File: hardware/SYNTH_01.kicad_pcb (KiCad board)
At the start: 2 copper layers, 55 parts, among them J2 Conn_01x04_Pin, SW1 SW_Push_45deg, SW10 SW_Push_45deg, SW11 SW_Push_45deg, SW12 SW_Push_45deg, SW13 SW_Push_45deg, SW14 SW_Push_45deg, SW15 SW_Push_45deg, SW16 SW_Push_45deg, SW17 SW_Push_45deg, SW18 SW_Push_45deg, SW19 SW_Push_45deg, SW2 SW_Push_45deg, SW20 SW_Push_45deg, SW21 SW_Push_45deg, SW3 SW_Push_45deg, SW4 SW_Push_45deg, SW5 SW_Push_45deg, SW6 SW_Push_45deg, SW7 SW_Push_45deg, SW8 SW_Push_45deg, SW9 SW_Push_45deg, U1 MCP23017-E/SP

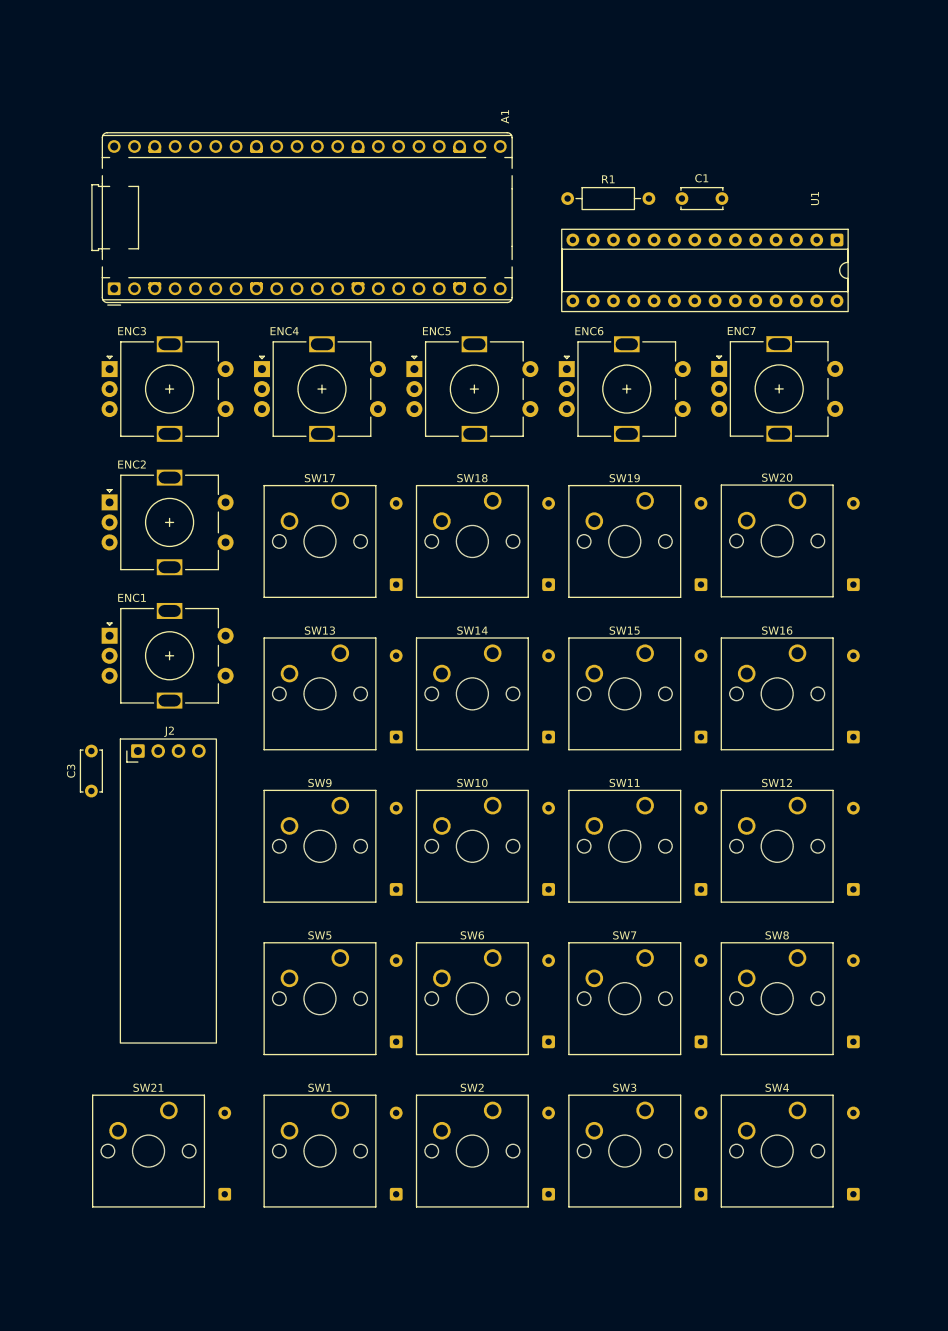
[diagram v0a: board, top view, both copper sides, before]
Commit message: PCB: linking encoders GND in PCB view, adding GND thermal to board
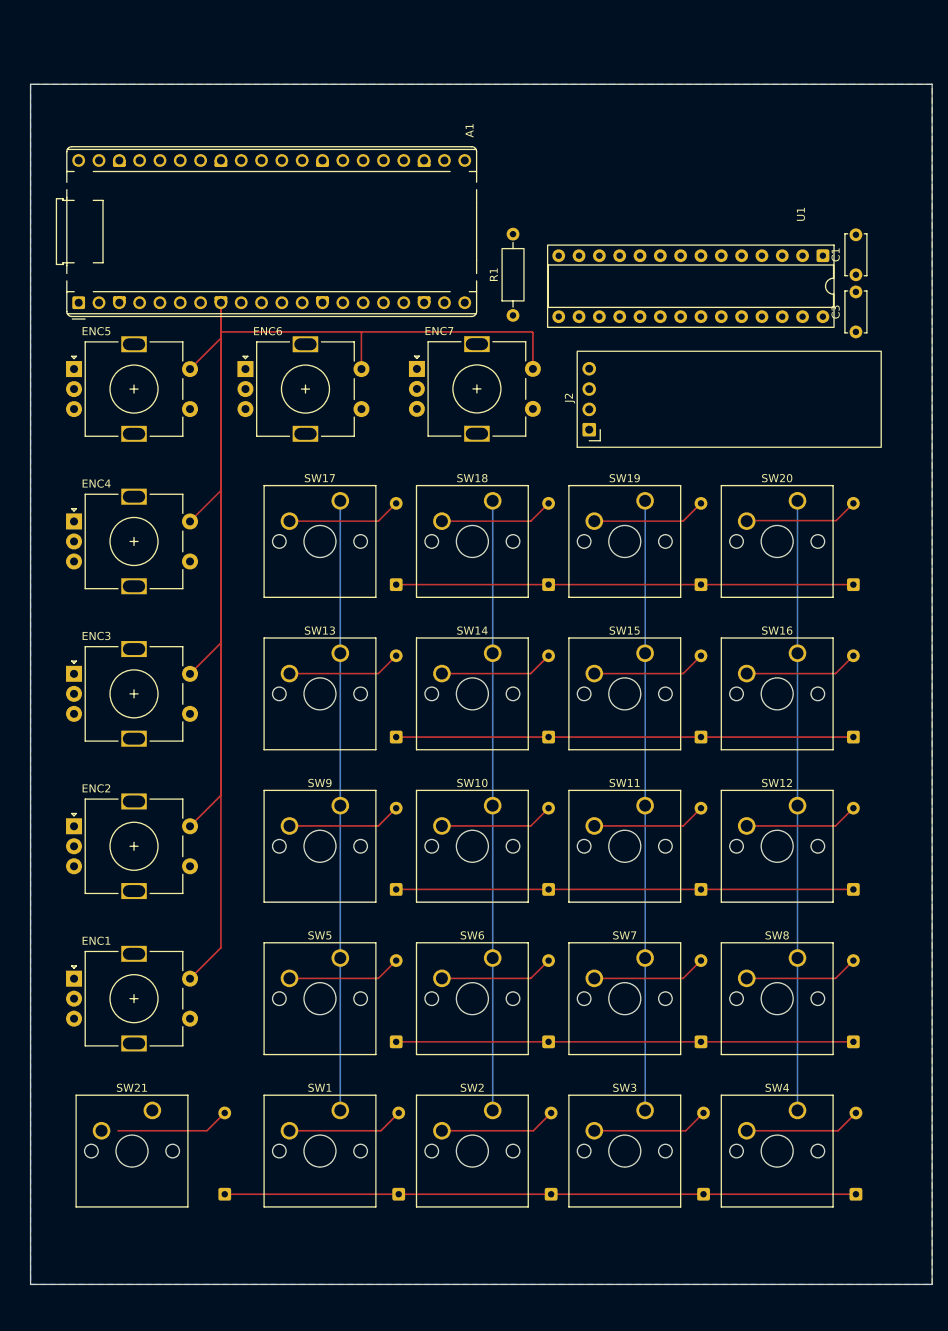
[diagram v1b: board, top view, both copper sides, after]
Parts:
- moved C3 111.5 mm to (147.6, 59.5)
- moved J2 69.3 mm to (114.3, 71.8), turned to 90 degrees
- moved D4 57.5 mm to (147.6, 167.3)
- moved D1 56.8 mm to (90.5, 167.3)
- moved ENC1 43.1 mm to (49.9, 140.4)
- moved ENC5 42.5 mm to (49.9, 64.2)
- moved ENC2 40.7 mm to (49.9, 121.3)
- moved ENC6 40.2 mm to (71.3, 64.2)
- moved ENC3 38.4 mm to (49.9, 102.3)
- moved ENC7 37.8 mm to (92.8, 64.2)
- moved ENC4 30.2 mm to (49.9, 83.2)
- moved C1 23.7 mm to (147.6, 52.4), turned to 90 degrees
- moved D3 19.4 mm to (128.6, 167.3)
- moved D2 18.7 mm to (109.5, 167.3)
- moved R1 16.1 mm to (104.8, 57.5), turned to 90 degrees
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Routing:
- net GND: track 0.00 -> 288.2 mm
- net /ROW4: track 0.00 -> 78.9 mm
- net /COL3: track 0.00 -> 76.3 mm
- net /COL2: track 0.00 -> 76.2 mm
- net /COL1: track 0.00 -> 76.2 mm
- net /COL0: track 0.00 -> 76.2 mm
- net /ROW3: track 0.00 -> 57.1 mm
- net /ROW2: track 0.00 -> 57.1 mm
- net /ROW1: track 0.00 -> 57.1 mm
- net /ROW0: track 0.00 -> 57.1 mm
- net Net-(D1-A): track 0.00 -> 14.6 mm
- net Net-(D3-A): track 0.00 -> 14.6 mm
- net Net-(D2-A): track 0.00 -> 14.6 mm
- net Net-(D4-A): track 0.00 -> 14.6 mm
- net Net-(D9-A): track 0.00 -> 14.3 mm
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- added copper zone on B.Cu, net GND
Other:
- board outline added: 112.7 x 150 mm

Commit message: fix: establish no-led PCB routing checkpoint
Prepare the pre-RGB SYNTH_01 variant on branch no_led for continued manual KiCad routing.\n\n- Add and wire the 4.7 kOhm DNP I2C pull-ups from +3V3 to SDA/SCL.\n- Validate the Pico/MCP power, reset, I2C and ground connections in the schematic.\n- Synchronize the PCB and route the power, I2C, reset and complete encoder subsystem.\n- Keep the RGB subsystem out of this buildable no-led variant.\n\nVerification at checkpoint time: schematic ERC reports 0 violations and schematic/PCB parity is clean. All 21 encoder nets are connected. PCB DRC reports 17 unconnected items: 10 matrix nets and 7 GND connections. It also reports 29 violations: 21 isolated-copper warnings, 4 starved-thermal warnings and 4 silkscreen overlaps. This checkpoint is not a fabrication release.
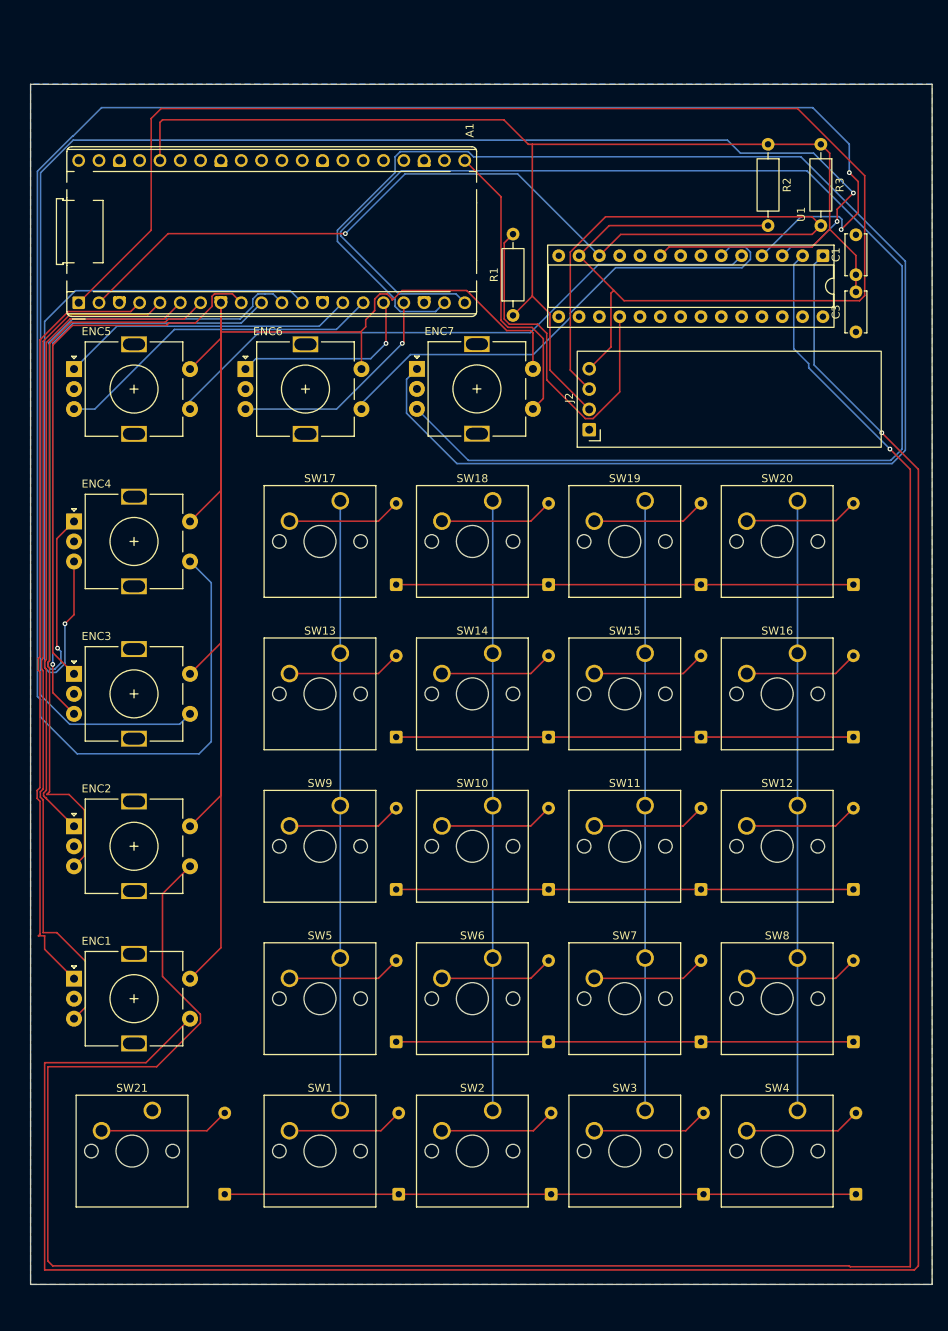
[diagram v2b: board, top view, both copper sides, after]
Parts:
- added R2: 4.7k, Resistor_THT:R_Axial_DIN0207_L6.3mm_D2.5mm_P10.16mm_Horizontal, F.Cu at (136.7, 36.1)
- added R3: 4.7k, Resistor_THT:R_Axial_DIN0207_L6.3mm_D2.5mm_P10.16mm_Horizontal, F.Cu at (143.3, 36.1)
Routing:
- net /E2_SW: track 0.00 -> 309.6 mm, vias 0 -> 1
- net /E1_SW: track 0.00 -> 287.9 mm, vias 0 -> 1
- net /E4_SW: track 0.00 -> 248.0 mm, vias 0 -> 2
- net /SDA: track 0.00 -> 209.5 mm
- net /E3_SW: track 0.00 -> 205.1 mm, vias 0 -> 2
- net /E7_A: track 0.00 -> 196.7 mm
- net /E7_B: track 0.00 -> 184.6 mm
- net +3V3: track 0.00 -> 171.1 mm
- net /SCL: track 0.00 -> 154.4 mm, vias 0 -> 1
- net /E1_B: track 0.00 -> 105.5 mm
- net /E1_A: track 0.00 -> 97.1 mm
- net /E4_B: track 0.00 -> 94.2 mm, vias 0 -> 1
- net /E4_A: track 0.00 -> 94.1 mm, vias 0 -> 1
- net /E2_B: track 0.00 -> 90.7 mm
- net /E2_A: track 0.00 -> 81.2 mm
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
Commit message: PCB: add 4 mounting holes and partial GND block (checkpoint for resume)
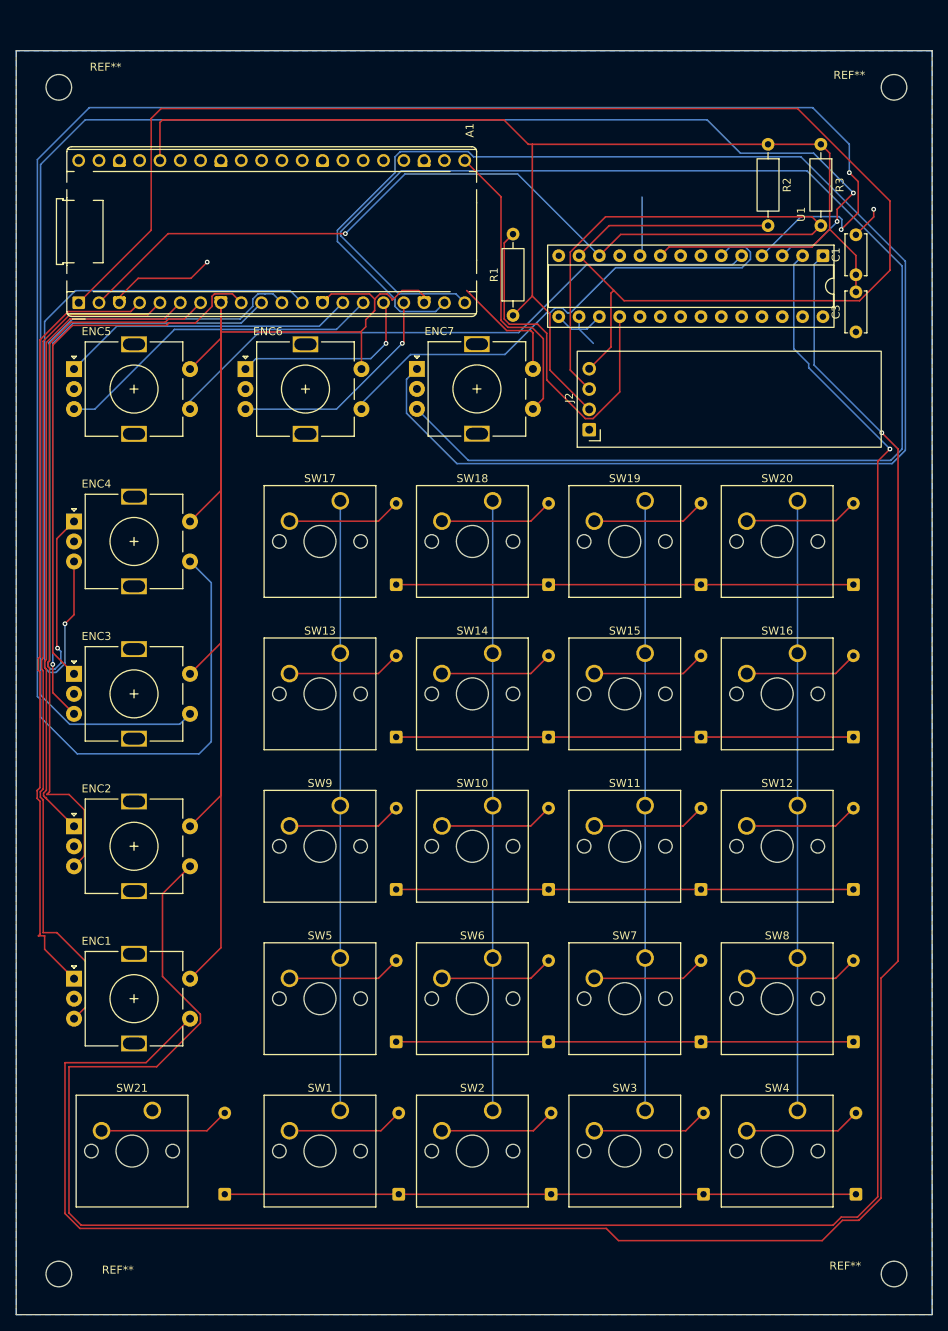
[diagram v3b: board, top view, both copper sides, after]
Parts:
- added REF**: MountingHole_3.2mm_M3, MountingHole:MountingHole_3.2mm_M3, F.Cu at (152.4, 177.3)
- added REF**: MountingHole_3.2mm_M3, MountingHole:MountingHole_3.2mm_M3, F.Cu at (48.0, 29.0)
- added REF**: MountingHole_3.2mm_M3, MountingHole:MountingHole_3.2mm_M3, F.Cu at (152.4, 29.0)
- added REF**: MountingHole_3.2mm_M3, MountingHole:MountingHole_3.2mm_M3, F.Cu at (48.0, 177.3)
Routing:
- net GND: track 294.6 -> 333.6 mm, vias 0 -> 2
- net /E2_SW: track 309.6 -> 286.9 mm
- net /E1_SW: track 287.9 -> 265.9 mm
- net /E3_SW: track 205.1 -> 207.8 mm
- net /SDA: track 209.5 -> 212.1 mm
- net /E4_SW: track 248.0 -> 248.9 mm
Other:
- board size 112.7 x 150 mm -> 114.5 x 158 mm

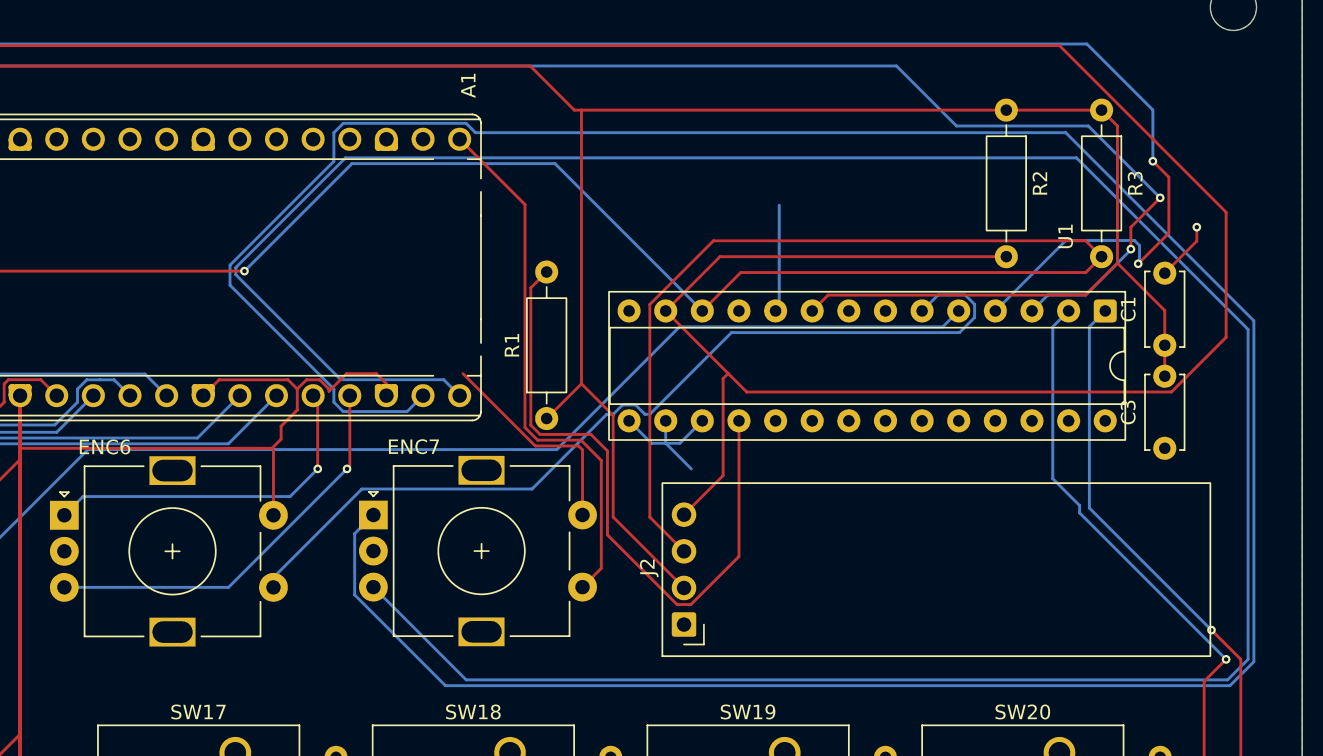
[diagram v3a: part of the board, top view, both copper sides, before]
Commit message: fix(pcb): consolidate GND-plane checkpoint
Remove floating B.Cu GND islands and complete the Pico ground return.

DRC checkpoint: 10 unrouted matrix nets remain; 6 starved thermals and 4
silkscreen overlaps remain. No GND missing connection, short circuit, or
dangling track remains. Resume by routing the matrix, then repair thermals
and silkscreen before Gerber review.
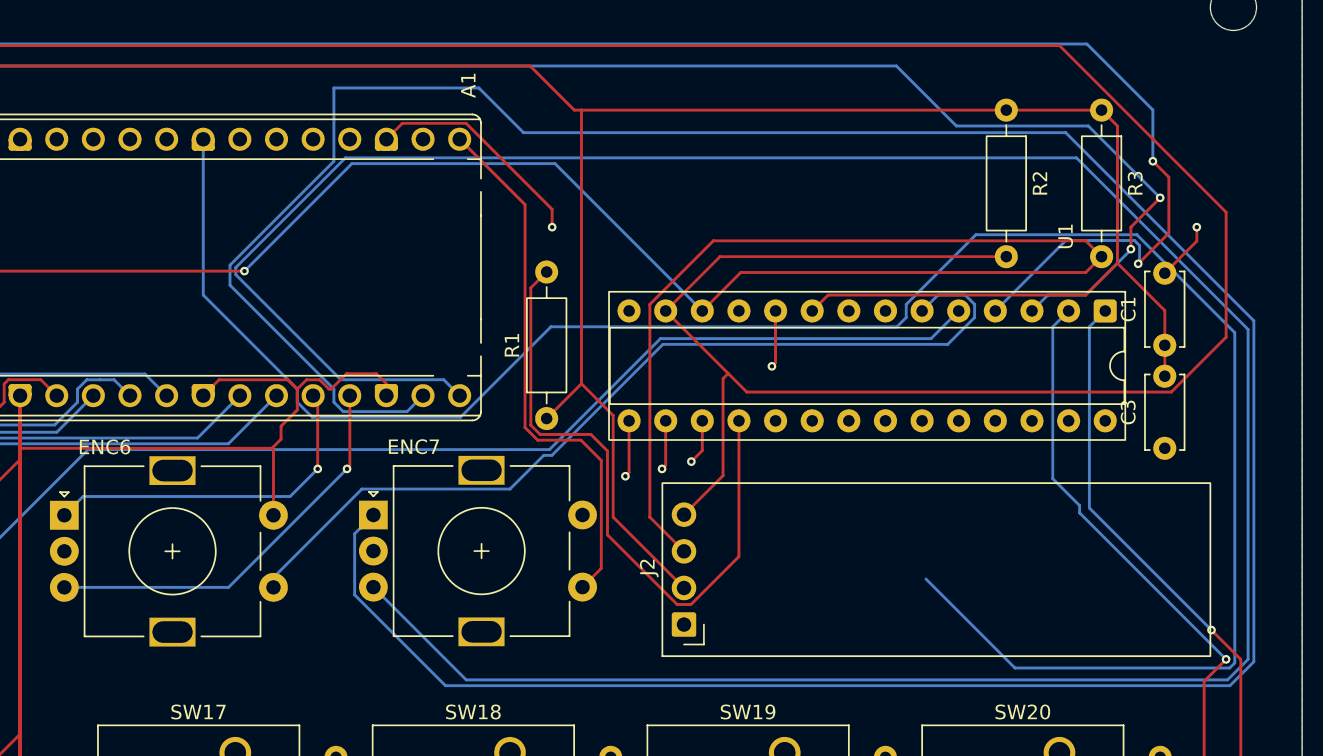
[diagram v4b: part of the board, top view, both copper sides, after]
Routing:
- net GND: track 333.6 -> 472.6 mm, vias 2 -> 7
- net /E7_A: track 196.7 -> 200.5 mm
- net /E6_SW: track 62.6 -> 62.0 mm
